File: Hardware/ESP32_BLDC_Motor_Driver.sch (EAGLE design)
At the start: 99 parts, among them J2 0532610371, J3 POWER_JACKPOWER_JACK_SLOT, J6 0.1in header, J7 QWIIC_RIGHT_ANGLE, Q1 20V/4.2A/52mΩ/1.4W, U1 TMC6300, U2 OPA344, U3 ESP-WROOM-3232D-NARROW, U4 CH340C, U5 ESD Diode, U6 AP63357, U7 AP63203

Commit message: Added datasheet, further changes from schematic review
See schematic review for more detailed changes: updated 3.3V LDO for an actual LDO, finished auto-reset circuitry, fixed pinout connections to breakout headers, changed size of logo, added qwiic logo, continued with layout. Datasheet added for the 3.3V LDO chosen.
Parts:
- removed C12: 10uF, SparkFun-Capacitors:10UF-0603-6.3V-20%
- removed FRAME2: FRAME-LETTER, SparkFun-Aesthetics:FRAME-LETTER
- removed L2: 4.7μH_SHIELDED_INDUCTOR, SparkFun-Coils:4.7μH_SHIELDED_INDUCTOR
- removed LOGO1: SFE_LOGO_NAME.5_INCH, SparkFun-Aesthetics:SFE_LOGO_NAME.5_INCH
- added LOGO5: SFE_LOGO_NAME.2_INCH, SparkFun-Aesthetics:SFE_LOGO_NAME.2_INCH
- added R24: 100k, SparkFun-Resistors:100KOHM-0603-1/10W-1%
- C10: value 22uF -> 1.0uF; device SparkFun-Capacitors:22UF-0603-6.3V-20% -> SparkFun-Capacitors:1.0UF-0603-16V-10%-X7R
- C11: value 22uF -> 100pF; device SparkFun-Capacitors:22UF-0603-6.3V-20% -> SparkFun-Capacitors:100PF-0603-50V-5%
- C9: value 0.1uF -> 2.2uF; device SparkFun-Capacitors:0.1UF-0603-25V-5% -> SparkFun-Capacitors:2.2UF-0603-10V-20%
- R22: value 100k -> 16.2k; device SparkFun-Resistors:100KOHM-0603-1/10W-1% -> SparkFun-Resistors:16.2KOHM-0603-1/10W-1%
- R23: value 100k -> 26.7k; device SparkFun-Resistors:100KOHM-0603-1/10W-1% -> SparkFun-Resistors:26.7KOHM0603-1/10W-1%
- U7: value AP63203 -> AP2202-ADJ; device SparkFun-IC-Power:AP63203 -> SparkFun-IC-Power:AP2202-ADJ
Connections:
- net ESP_15 renamed ESP_15/GPIO4
- net ESP_16 renamed N$18
- net N$12 renamed TP2
- net N$16 renamed POWER_IN
- removed net ESP_0: J4.7
- removed net ESP_13: J4.5, U3.PICO2/IOA13
- removed net ESP_17: J5.2, U3.IO17
- removed net ESP_18: J5.4, U3.SCK3/IO18
- removed net ESP_19: J5.5
- removed net ESP_2: J4.8, U3.IOA2
- removed net ESP_21: J5.6
- removed net ESP_22: J5.7
- removed net ESP_34: D2.DI, J4.3
- removed net ESP_35: J4.4
- removed net ESP_36: J4.1, U3.SENSOR_VP/IA36
- removed net ESP_39: J4.2, U3.SENSOR_VN/IA39
- removed net N$10: C9.1, U7.BST
- removed net N$13: C11.2
- removed net N$9: C9.2, L2.1, U7.SW
- new net EN_MOTOR: R17.1, U3.IO16, U6.EN
- new net ESP_12/GPIO1: J4.7, U3.POCI2/IOA12
- new net ESP_36/LED: D2.DI, J5.6, U3.SENSOR_VP/IA36
- new net ESP_39/TP_A3: J5.5, U3.SENSOR_VN/IA39
- new net ESP_4: J4.5, U3.IOA4
- new net N$16: J5.2
- net !RESET: now also J5.3
- net !STDBY: now also U3.IOA2
- net 3.3V_LDO: now also C9.1, R22.2, U7.OUT; no longer C10.1, C11.1, L2.2, U7.FB
- net CURR_SENSE: now also J5.4
- net DIAG: now also U3.SCK3/IO18; no longer U3.IOA4
- net EN: now also R24.1, U3.IO17, U7.EN; no longer R17.1, U3.IO16, U6.EN
- net ESP_19/POCI: now also J4.4
- net ESP_21/TP_SDA: now also J4.2
- net ESP_22/TP_SCL: now also J4.1
- net ESP_23/PICO: now also J4.3; no longer J5.8
- net ESP_34/AUX1: now also J5.8
- net ESP_35/AUX2: now also J5.7
- net ESP_5: now also J4.8; no longer J5.3
- net GND: now also C11.2, C9.2; no longer C12.2
- net N$2: now also C11.1, U7.ADJ; no longer U7.EN
- net UH: now also U3.PICO2/IOA13; no longer U3.POCI2/IOA12
- net VIN: now also C10.1, R24.2, U7.IN; no longer C12.1, R22.2, U7.VIN
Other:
- note added: "Boot and Reset Buttons"
- note removed: "4.7uH"
- note removed: "GPIO0 and Reset Buttons"
- moved on the sheet: C10, C11, C4, C7, C9, D2, J4, J5, J7, R22, R23, TP2

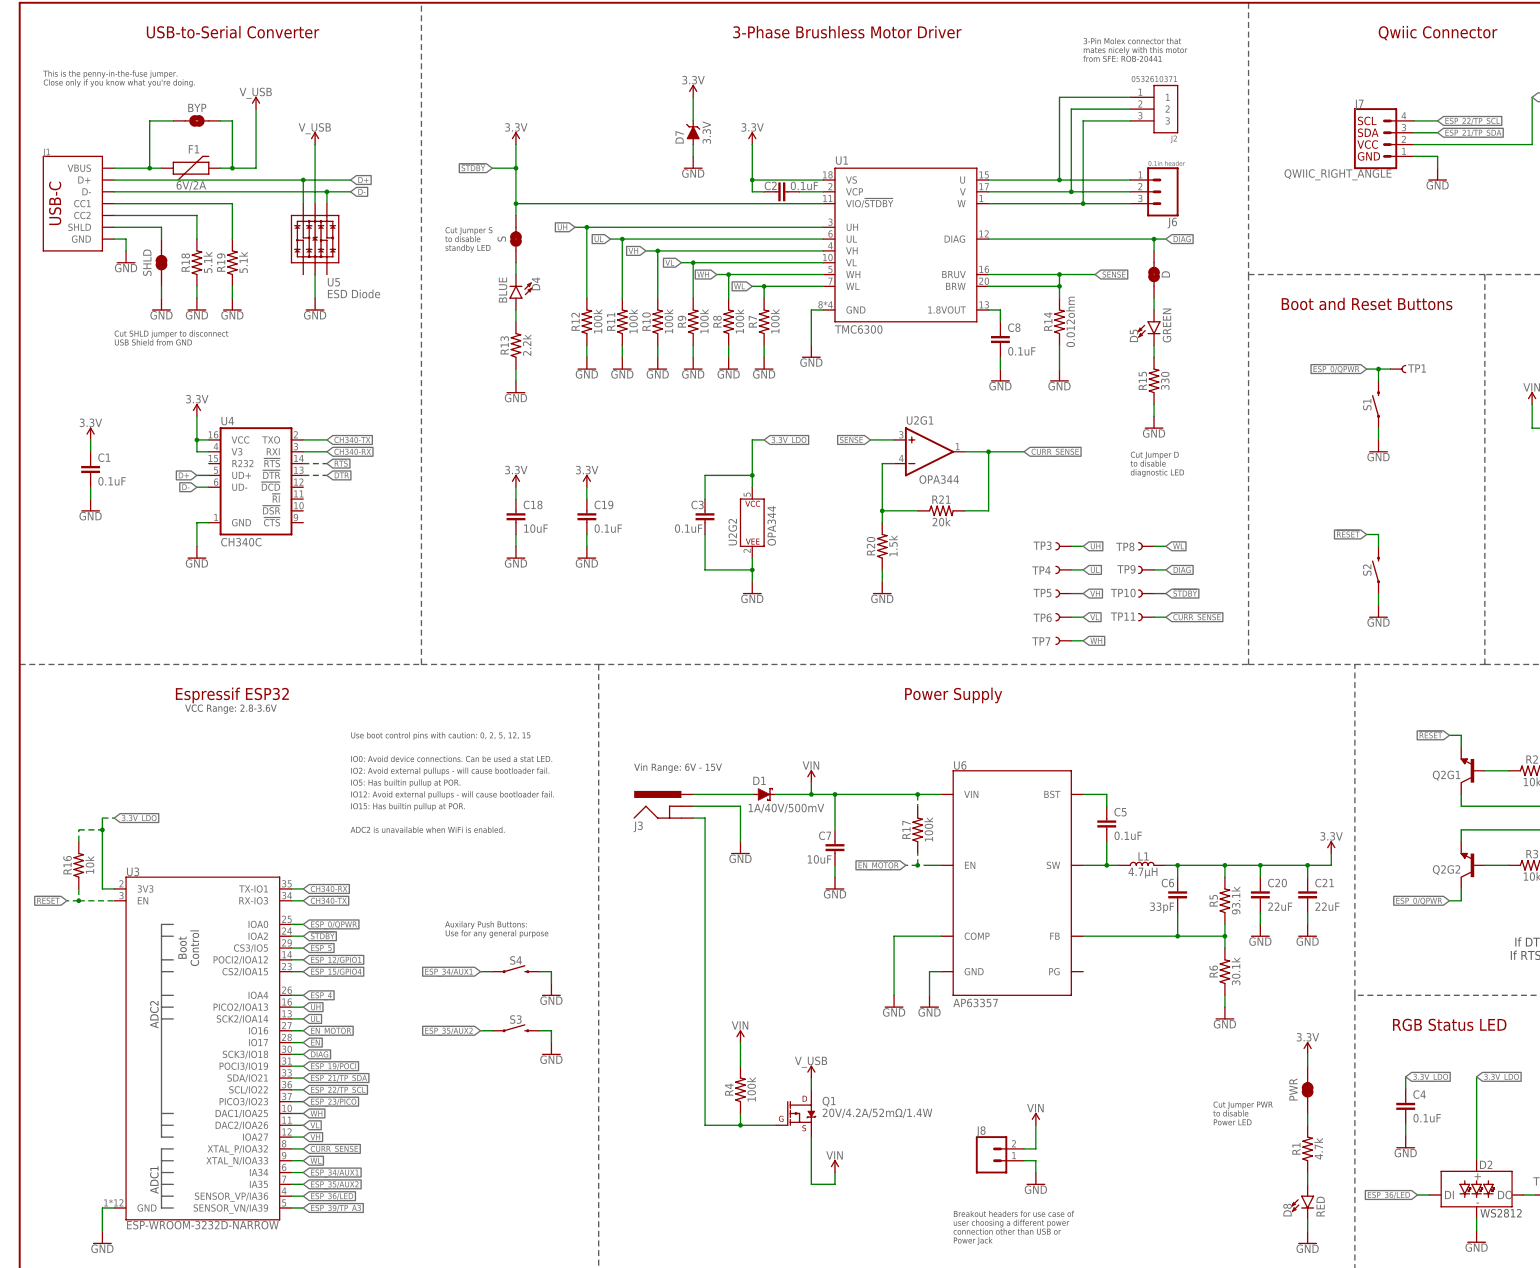
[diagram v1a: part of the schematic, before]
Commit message: Continue with design
Adjusted schematic components for better routing. Continued routing design - still a lot left to complete.
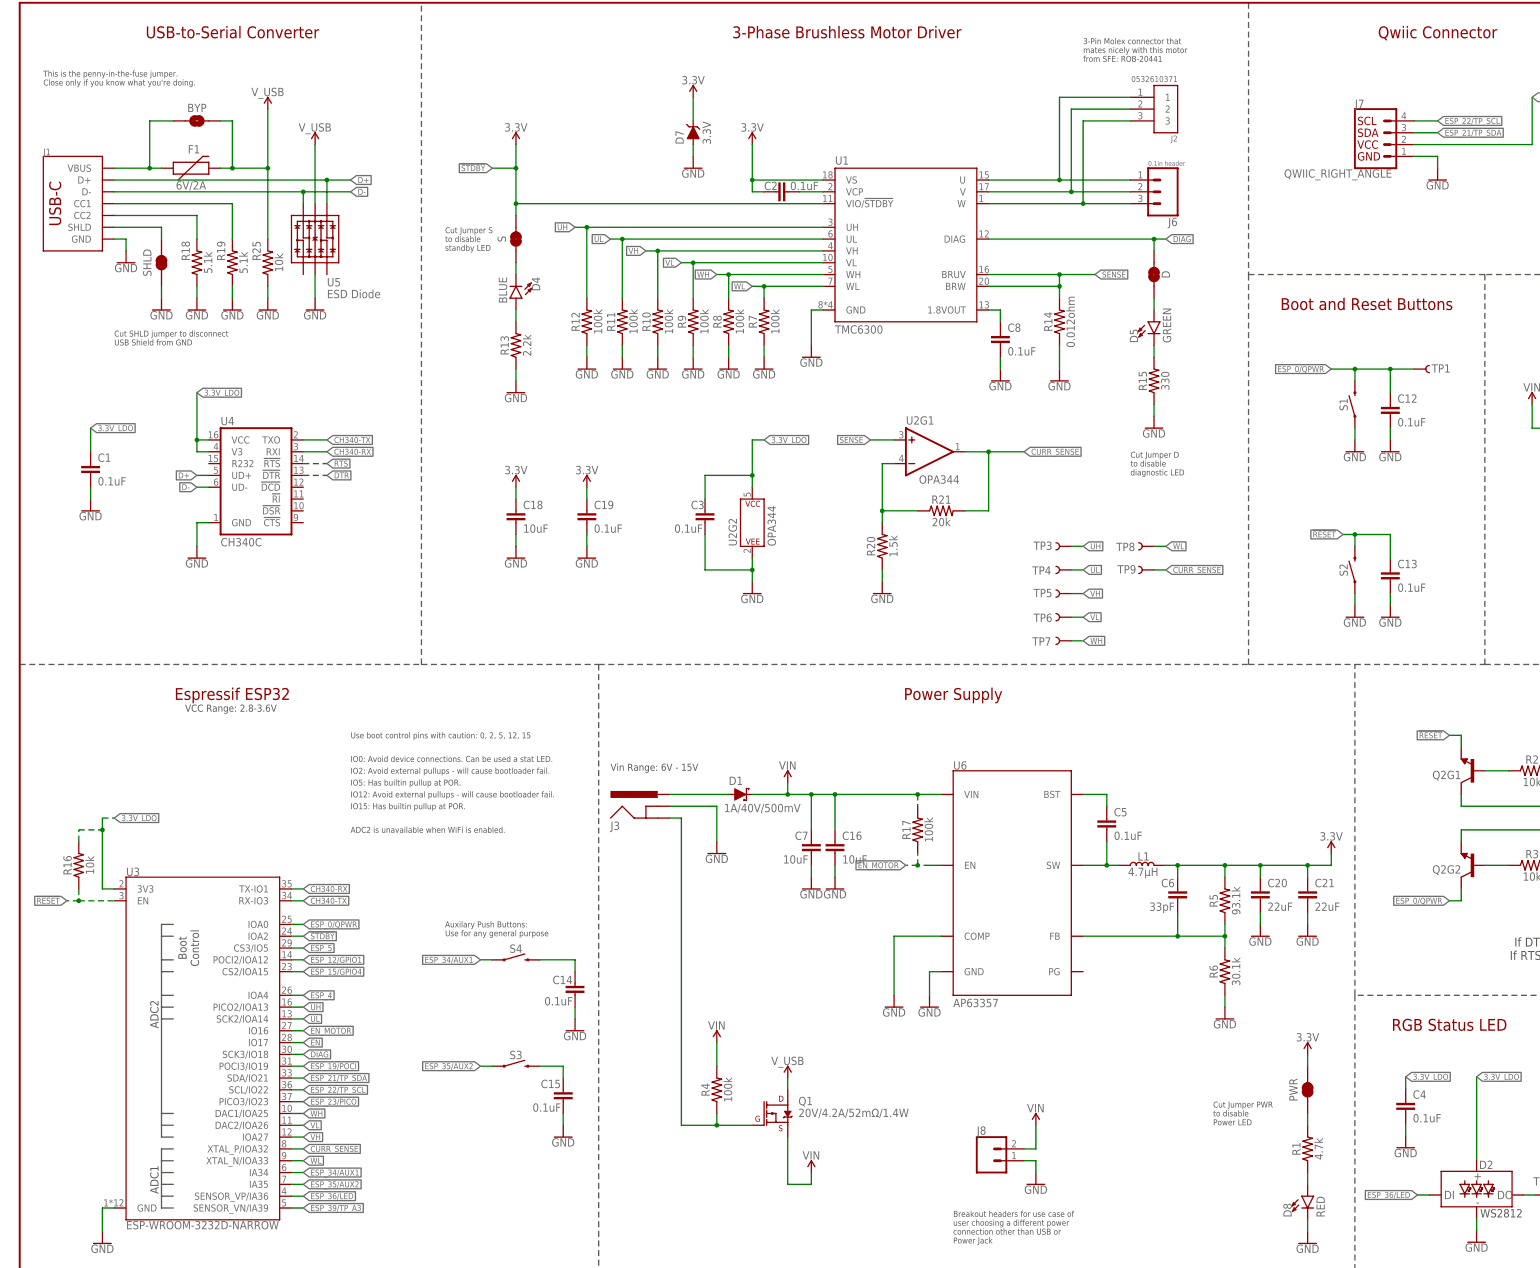
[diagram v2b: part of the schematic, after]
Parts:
- removed TP10, TP11: TEST-POINT3X4, SparkFun-Connectors:TEST-POINT3X4
- added C12, C13, C14, C15: 0.1uF, SparkFun-Capacitors:0.1UF-0603-25V-(+80/-20%)
- added C16: 10uF, SparkFun-Capacitors:10UF-0603-6.3V-20%
- added R25: 10k, SparkFun-Resistors:10KOHM-0603-1/10W-1%
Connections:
- net N$21 renamed BST
- net N$22 renamed SW
- net N$28 renamed S
- net N$30 renamed 1.8_VOUT
- net N$32 renamed D
- net N$36 renamed FB
- new net N$10: C14.1, S4.2
- new net N$9: C15.1, S3.2
- net !RESET: now also C13.1
- net !STDBY: no longer TP10.1
- net 3.3V: no longer C1.1, U4.V3, U4.VCC
- net 3.3V_LDO: now also C1.1, U4.V3, U4.VCC
- net CURR_SENSE: now also TP9.1; no longer TP11.1
- net D+: now also U5.IO3; no longer U5.IO4
- net D-: now also U5.IO4; no longer U5.IO3
- net DIAG: no longer TP9.1
- net ESP_0/QPWR: now also C12.1
- net GND: now also C12.2, C13.2, C14.2, C15.2, C16.2, R25.1; no longer S3.2, S4.2
- net VIN: now also C16.1
- net V_USB: now also R25.2
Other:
- moved on the sheet: C7, D1, J3, Q1, R4, S1, S2, S3, S4, TP1

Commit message: Continued work on layout
Added polygons to layout, added layers 2,15, continued with routing
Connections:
- net U: now also J2.3, J6.3; no longer J2.1, J6.1
- net W: now also J2.1, J6.1; no longer J2.3, J6.3
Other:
- moved on the sheet: J2, J6
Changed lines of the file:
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@@
 <attribute name="VALUE" x="278.384" y="33.02" size="1.778" layer="96" font="vector" rot="R90" align="top-center"/>
 </instance>
-<instance part="J2" gate="G$1" x="246.38" y="256.54" smashed="yes" rot="MR0">
-<attribute name="NAME" x="248.926859375" y="249.57043125" size="1.27343125" layer="95" rot="MR0"/>
-<attribute name="VALUE" x="248.92545" y="262.36565" size="1.27273125" layer="96" rot="MR0"/>
-</instance>
-<instance part="J6" gate="J$1" x="246.38" y="238.76" smashed="yes" rot="R180">
-<attribute name="VALUE" x="242.57" y="244.348" size="1.016" layer="96" font="vector"/>
-<attribute name="NAME" x="248.92" y="233.172" size="1.778" layer="95" font="vector" rot="R180"/>
+<instance part="J2" gate="G$1" x="246.38" y="256.54" smashed="yes" rot="R180">
+<attribute name="NAME" x="248.926859375" y="263.50956875" size="1.27343125" layer="95" rot="R180"/>
+<attribute name="VALUE" x="248.92545" y="250.71435" size="1.27273125" layer="96" rot="R180"/>
+</instance>
+<instance part="J6" gate="J$1" x="246.38" y="238.76" smashed="yes" rot="MR0">
+<attribute name="VALUE" x="242.57" y="233.172" size="1.016" layer="96" font="vector" rot="MR180"/>
+<attribute name="NAME" x="248.92" y="244.348" size="1.778" layer="95" font="vector" rot="MR0"/>
 </instance>
 <instance part="R2" gate="G$1" x="325.12" y="114.3" smashed="yes">
@@
 <wire x1="208.28" y1="236.22" x2="228.6" y2="236.22" width="0.1524" layer="91"/>
 <wire x1="228.6" y1="236.22" x2="228.6" y2="254" width="0.1524" layer="91"/>
-<wire x1="228.6" y1="236.22" x2="238.76" y2="236.22" width="0.1524" layer="91"/>
+<pinref part="J2" gate="G$1" pin="1"/>
+<wire x1="228.6" y1="254" x2="238.76" y2="254" width="0.1524" layer="91"/>
+<pinref part="J6" gate="J$1" pin="1"/>
+<wire x1="238.76" y1="236.22" x2="228.6" y2="236.22" width="0.1524" layer="91"/>
 <junction x="228.6" y="236.22"/>
-<pinref part="J2" gate="G$1" pin="3"/>
-<wire x1="228.6" y1="254" x2="238.76" y2="254" width="0.1524" layer="91"/>
-<pinref part="J6" gate="J$1" pin="3"/>
 </segment>
 </net>
@@
 <wire x1="226.06" y1="238.76" x2="208.28" y2="238.76" width="0.1524" layer="91"/>
 <wire x1="226.06" y1="238.76" x2="226.06" y2="256.54" width="0.1524" layer="91"/>
-<wire x1="226.06" y1="238.76" x2="238.76" y2="238.76" width="0.1524" layer="91"/>
-<junction x="226.06" y="238.76"/>
 <pinref part="J2" gate="G$1" pin="2"/>
 <wire x1="238.76" y1="256.54" x2="226.06" y2="256.54" width="0.1524" layer="91"/>
 <pinref part="J6" gate="J$1" pin="2"/>
+<wire x1="226.06" y1="238.76" x2="238.76" y2="238.76" width="0.1524" layer="91"/>
+<junction x="226.06" y="238.76"/>
 </segment>
 </net>
@@
 <wire x1="208.28" y1="241.3" x2="223.52" y2="241.3" width="0.1524" layer="91"/>
 <wire x1="223.52" y1="241.3" x2="223.52" y2="259.08" width="0.1524" layer="91"/>
+<pinref part="J2" gate="G$1" pin="3"/>
+<wire x1="238.76" y1="259.08" x2="223.52" y2="259.08" width="0.1524" layer="91"/>
+<pinref part="J6" gate="J$1" pin="3"/>
+<wire x1="223.52" y1="241.3" x2="238.76" y2="241.3" width="0.1524" layer="91"/>
 <junction x="223.52" y="241.3"/>
-<pinref part="J2" gate="G$1" pin="1"/>
-<wire x1="238.76" y1="259.08" x2="223.52" y2="259.08" width="0.1524" layer="91"/>
-<pinref part="J6" gate="J$1" pin="1"/>
-<wire x1="223.52" y1="241.3" x2="238.76" y2="241.3" width="0.1524" layer="91"/>
-</segment>
-</net>
+</segment>
+</net>

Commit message: Updates to library and schematic
Added decoupling caps to ESP32 as per the datasheet, updated the library for the magnetic encoder for better schematic routing, moved components on the board for layout, made small changes/fixes to schematic for net label names and for the breakout header
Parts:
- added C17: 0.1uF, SparkFun-Capacitors:0.1UF-0603-25V-5%
- added C22: 22uF, SparkFun-Capacitors:22UF-0603-6.3V-20%
- added C23: 0.1uF, SparkFun-Capacitors:0.1UF-0402-10V-10%-X7R
- added I2C: JUMPER-SMT_3_2-NC_TRACE_SILK, SparkFun-Jumpers:JUMPER-SMT_3_2-NC_TRACE_SILK
- added INT: JUMPER-SMT_2_NC_TRACE_SILK, SparkFun-Jumpers:JUMPER-SMT_2_NC_TRACE_SILK
- added R26, R27: 2.2k, SparkFun-Resistors:2.2KOHM-0603-1/10W-1%
- added R28: 10k, SparkFun-Resistors:10KOHM-0603-1/10W-1%
- added U8: TMAG5273, TMAG5273:TMAG5273A1QDBVT
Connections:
- net CURR_SENSE renamed ESP_32/CURR_SENSE
- net DIAG renamed ESP_18/DIAG
- net EN renamed ESP_17/EN
- net EN_MOTOR renamed ESP_16/EN_MOTOR_PWR
- net ESP_4 renamed ESP_4/GPIO4
- net ESP_5 renamed ESP_5/GPIO5
- net UH renamed ESP_13/UH
- net UL renamed ESP_14/UL
- net VH renamed ESP_27/VH
- net VL renamed ESP_26/VL
- net WH renamed ESP_25/WH
- net WL renamed ESP_33/WL
- new net !INT: R28.1, U8.!INT
- new net ESP_0/!STDBY: U3.IOA2
- new net N$11: INT.1, R28.2
- new net N$12: I2C.3, R27.2
- new net N$13: I2C.1, R26.2
- net !STDBY: no longer U3.IOA2
- net 3.3V_LDO: now also C17.1, C22.1, C23.1, I2C.2, INT.2, U8.VCC
- net ESP_21/TP_SDA: now also R26.1, U8.SDA
- net ESP_22/TP_SCL: now also R27.1, U8.SCL
- net GND: now also C17.2, C22.2, C23.2, U8.GND, U8.GND(TEST)
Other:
- note added: "Magnetic Encoder"
- moved on the sheet: C1, C10, C11, C12, C13, C14, C15, C16, C18, C19, C20, C21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

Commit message: Design updates for board and schematic
Continued work from schematic and layout - not complete, needs more routing and placement adjustments.
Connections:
- removed net !INT: R28.1, U8.!INT
- removed net !STDBY: S.2, U1.VIO/!STDBY!
- removed net ESP_4/GPIO4: J4.5, U3.IOA4
- removed net N$16: J5.2
- new net ESP_4/!INT: J4.5, R28.1, U3.IOA4, U8.!INT
- net ESP_0/!STDBY: now also J5.2, S.2, U1.VIO/!STDBY!
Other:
- moved on the sheet: C18, C19, C2, C23, C3, C8, D, D4, D5, D7, I2C, INT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

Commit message: Addition of motor footprint to library; updates to schematic and layout
Opened up layout of the board for addition of milling layer; broke out power good signal to the breakout headers; adjusted auxilary buttons for proper use; adjusted VIO to be configured correctly; changed note for copper weight usage; created footprint for the motor
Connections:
- removed net N$10: C14.1, S4.2
- removed net N$18: J5.1
- removed net N$9: C15.1, S3.2
- new net 3.3V_PG: J5.1, U6.PG
- net ESP_34/AUX1: now also C14.1, S4.2; no longer S4.1
- net ESP_35/AUX2: now also C15.1, S3.2; no longer S3.1
- net GND: now also S3.1, S4.1
- net N$29: now also D4.C; no longer D4.A
- net S: now also D4.A; no longer D4.C
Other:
- note added: "Hall-Effect Sensor"
- note added: "Power Supply - LDO"
- note removed: "Isolated Power Supply"
- note removed: "Magnetic Encoder"
- moved on the sheet: C14, C15, C17, C22, C23, C4, D4, I2C, INT, R26, R27, R28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

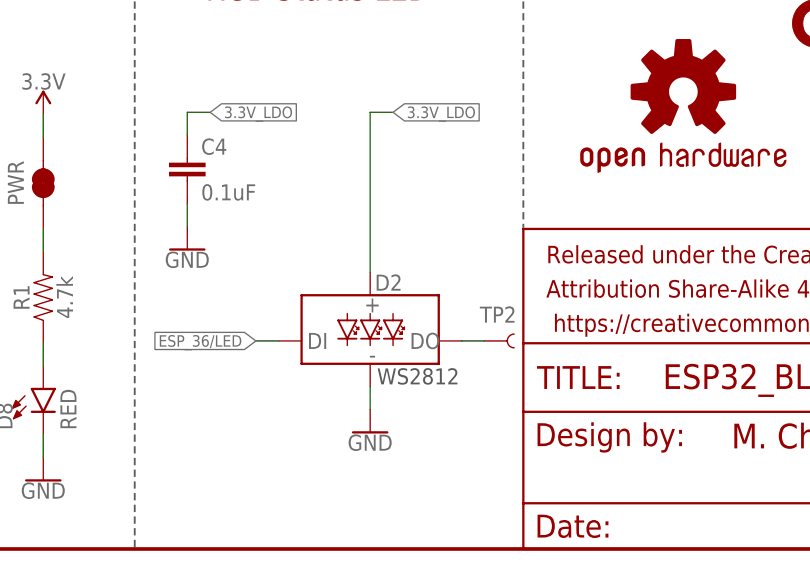
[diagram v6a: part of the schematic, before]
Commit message: Layout Updates
Completed all air wires and most design rule errors - still a few to go. Layout primarily solidified. logos, name, and labels added to board.
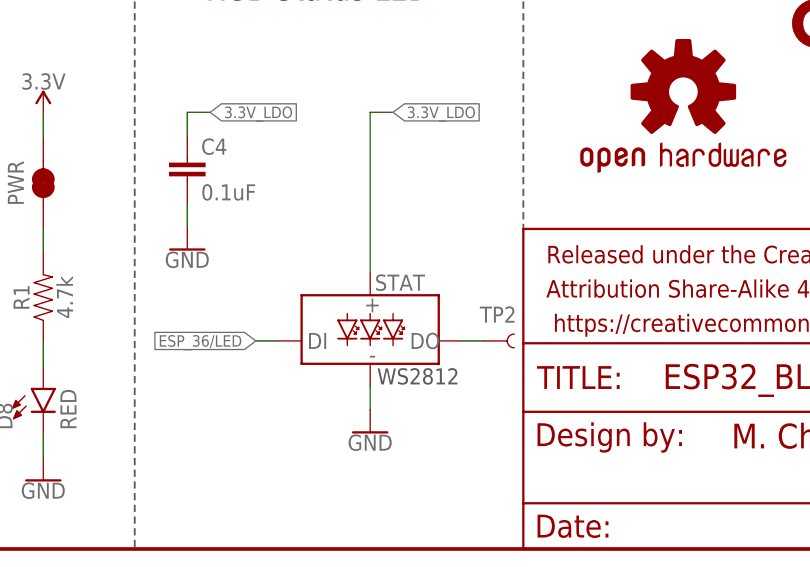
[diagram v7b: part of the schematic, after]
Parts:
- J1: value (none) -> USB-C Connector
- J4: value (none) -> Breadboard Connector
- J5: value (none) -> Breadboard Headers
- J8: value (none) -> Breakout Header
- LOGO3: value SFE_LOGO_FLAME.5_INCH -> SFE_LOGO_FLAME.3_INCH; device SparkFun-Aesthetics:SFE_LOGO_FLAME.5_INCH -> SparkFun-Aesthetics:SFE_LOGO_FLAME.3_INCH
- LOGO5: value SFE_LOGO_NAME.2_INCH -> SFE_LOGO_NAME.1_INCH; device SparkFun-Aesthetics:SFE_LOGO_NAME.2_INCH -> SparkFun-Aesthetics:SFE_LOGO_NAME.1_INCH
- Q2: value (none) -> NPN Transistors
- renumbered D2 to STAT

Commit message: Design Updates
Further work done on inline current sensing - restarting computer
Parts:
- removed U2: OPA344, SparkFun-IC-Amplifiers:OPA344
- added U9: LMV324, SparkFun-IC-Amplifiers:LMV324
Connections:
- new net N$14: R20.2, R21.1, U9G1.+IN
- net 3.3V_LDO: now also U9G5.P$V+; no longer U2G2.P$V+
- net ESP_32/CURR_SENSE: now also U9G1.OUT; no longer U2G1.OUT
- net GND: now also U9G5.P$V-; no longer U2G2.P$V-
- net N$6: now also U9G2.-IN; no longer R20.2, R21.1, U2G1.-IN
- net SENSE: now also U9G1.-IN; no longer U2G1.+IN
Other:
- note added: "Maximum Input Current: 0.5A"
- moved on the sheet: C18, C19, C2, C3, C8, D, D4, D5, D7, J2, J6, R10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
